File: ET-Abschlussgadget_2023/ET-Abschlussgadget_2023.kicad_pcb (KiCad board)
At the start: 2 copper layers, 85 x 54 mm, 26 parts, among them SW1 ON/OFF, U1 ATtiny10-TS

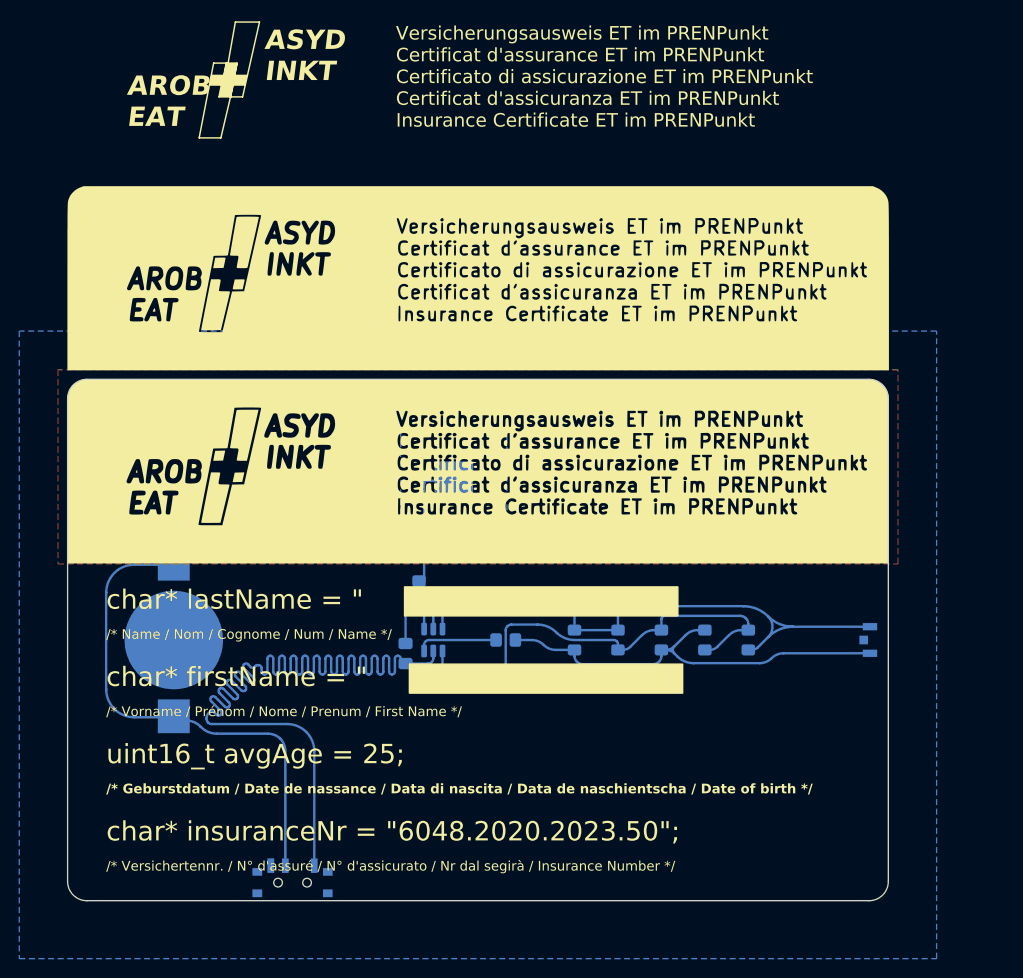
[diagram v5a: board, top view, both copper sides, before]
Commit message: Add material-list, Adjust footprints, add first datasheets
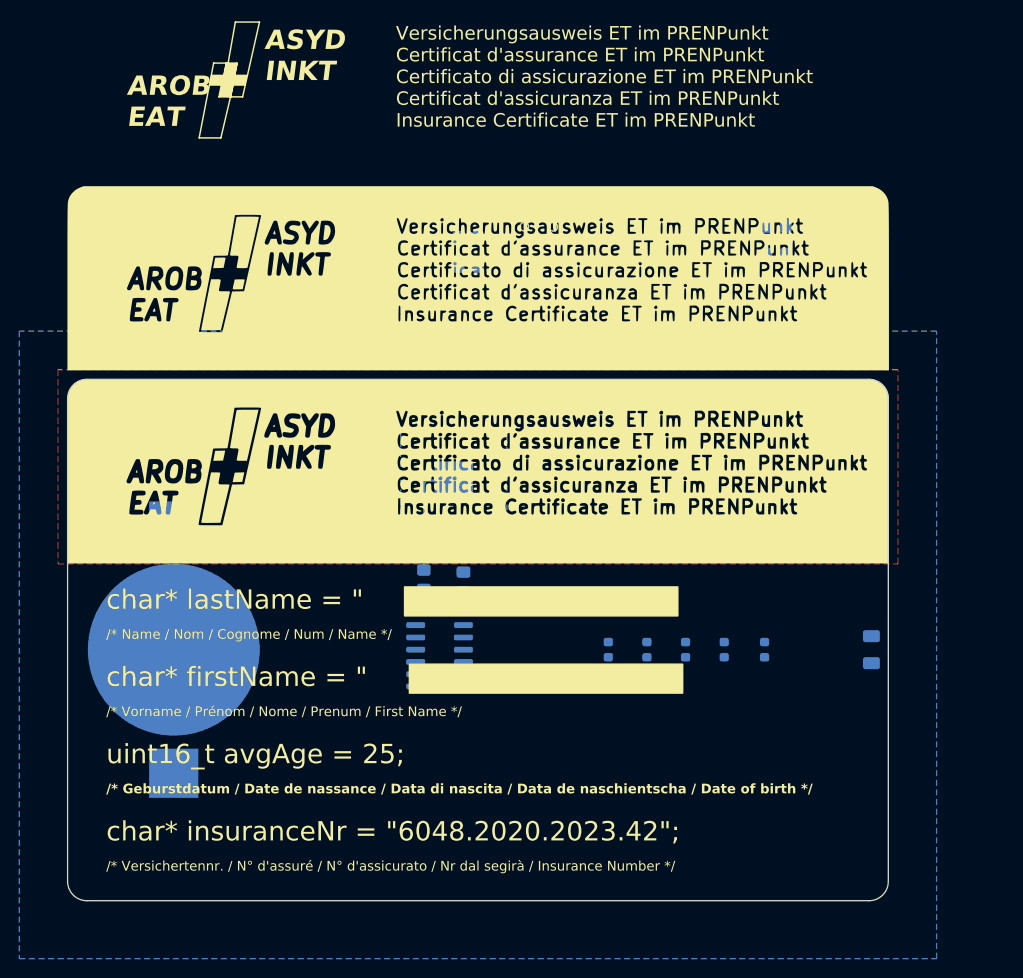
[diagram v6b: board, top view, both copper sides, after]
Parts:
- added J1: PB0, TestPoint:TestPoint_Pad_D1.0mm, B.Cu at (110.0, 83.0)
- added J2: PB1, TestPoint:TestPoint_Pad_D1.0mm, B.Cu at (112.0, 83.0)
- added J3: UPDI / RESET, TestPoint:TestPoint_Pad_D2.0mm, B.Cu at (107.0, 83.0)
- added J4: EXTCLK, TestPoint:TestPoint_Pad_D2.0mm, B.Cu at (103.0, 83.0)
- added R4: 590, Resistor_SMD:R_0805_2012Metric_Pad1.20x1.40mm_HandSolder, B.Cu at (173.4, 64.1)
- added R6: 590, Resistor_SMD:R_0805_2012Metric_Pad1.20x1.40mm_HandSolder, B.Cu at (173.4, 67.1)
- added R7: 590, Resistor_SMD:R_0805_2012Metric_Pad1.20x1.40mm_HandSolder, B.Cu at (141.5, 68.3)
- BT1: footprint Battery:BatteryHolder_Keystone_3000_1x12mm -> Battery:BatteryHolder_Keystone_3002_1x2032
- D1, D3, D4, D5: footprint LED_SMD:LED_0805_2012Metric_Pad1.15x1.40mm_HandSolder -> LED_SMD:LED_0603_1608Metric
- D2: value LED_Red -> LED_Ir; footprint LED_SMD:LED_0805_2012Metric_Pad1.15x1.40mm_HandSolder -> LED_SMD:LED_1206_3216Metric
- D6: value LED_Ir -> LED_Red; footprint LED_SMD:LED_LiteOn_LTST-S326 -> LED_SMD:LED_0603_1608Metric
- R1, R2, R3: value 220R -> 590
- R5: renamed from R4; value 1k -> 590
- U1: value ATtiny10-TS -> ATtiny414-SS; footprint Package_TO_SOT_SMD:SOT-23-6 -> Package_SO:SOIC-14_3.9x8.7mm_P1.27mm
- moved SW1 72.6 mm to (148.8, 63.9)
- moved R3 53.7 mm to (173.4, 61.2), turned to 180 degrees
- moved R2 45.3 mm to (141.5, 65.3), turned to 180 degrees
- moved R1 41.3 mm to (141.5, 62.4), turned to 180 degrees
- moved D2 17.3 mm to (183.2, 108.0), turned to -90 degrees
- moved D5 15.5 mm to (168.0, 108.0), turned to -90 degrees
- moved D1 14.5 mm to (156.0, 108.0), turned to -90 degrees
- moved D6 11.0 mm to (172.2, 108.0), turned to -90 degrees
- moved C1 9.53 mm to (141.0, 101.0)
- moved D4 7.07 mm to (164.0, 108.0), turned to -90 degrees
- moved D3 1.80 mm to (160.0, 108.0), turned to -90 degrees
- moved R5 1.25 mm to (136.9, 100.8)
- moved U1 1.19 mm to (138.5, 108.0), turned to 180 degrees
- moved BT1 1.00 mm to (111.0, 108.0), turned to 90 degrees
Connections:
- D1 pad 2: Net-(D1-A) -> GND
- D2 pad 1: Net-(D1-A) -> Net-(D2-K)
- D2 pad 2: Net-(D2-A) -> GND
- D3 pad 1: Net-(D2-A) -> Net-(D3-K)
- D3 pad 2: Net-(D1-A) -> GND
- D4 pad 1: Net-(D1-A) -> Net-(D4-K)
- D4 pad 2: Net-(D1-K) -> GND
- D5 pad 1: Net-(D2-A) -> Net-(D5-K)
- D5 pad 2: Net-(D1-K) -> GND
- D6 pad 1: Net-(D1-K) -> Net-(D6-K)
- D6 pad 2: Net-(D2-A) -> GND
- R1 pad 1: Net-(U1-PB1) -> Net-(D1-K)
- R1 pad 2: Net-(D1-K) -> /LED 1
- R2 pad 1: Net-(U1-PB2) -> Net-(D2-K)
- R2 pad 2: Net-(D1-A) -> /LED IR
- R3 pad 1: Net-(U1-~{RESET}/PB3) -> /LED 2
- R3 pad 2: Net-(D2-A) -> Net-(D3-K)
- R5 pad 1: Net-(U1-PB0) -> /Cap_Pad / ADC1
- SW1 pad : GND -> (no net)
- U1 pad 1: Net-(U1-PB0) -> VCC
- U1 pad 2: GND -> /LED 5
- U1 pad 3: Net-(U1-PB1) -> /LED 4
- U1 pad 4: Net-(U1-PB2) -> /LED 3
- U1 pad 5: VCC -> /LED 2
- U1 pad 6: Net-(U1-~{RESET}/PB3) -> /LED IR
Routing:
- net VCC: track 107.4 -> 0.00 mm
- net Net-(BT1-+): track 51.5 -> 0.00 mm
- net Net-(D1-K): track 49.6 -> 0.00 mm
- net Net-(D2-A): track 45.1 -> 0.00 mm
- net Net-(D1-A): track 40.2 -> 0.00 mm
- net GND: track 11.9 -> 0.00 mm
- net Net-(U1-~{RESET}/PB3): track 8.36 -> 0.00 mm
- net Net-(U1-PB1): track 7.71 -> 0.00 mm
- net Net-(U1-PB2): track 7.71 -> 0.00 mm
- net Net-(U1-PB0): track 3.14 -> 0.00 mm
- net /Cap_Pad: track 13.3 -> 12.4 mm
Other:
- board text added: "char* insuranceNr = {dblquote}6048.2020.2023.42{dblquote};"
- board text removed: "char* insuranceNr = {dblquote}6048.2020.2023.50{dblquote};"
